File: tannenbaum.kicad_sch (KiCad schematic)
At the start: 34 parts, among them Q1 MMBT3904-7-F, Q2 MMBT3904-7-F, Q3 MMBT3904-7-F, Q4 MMBT3904-7-F, Q5 2N7002, U1 ICM7555IPAZ

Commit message: nets
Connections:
- net V2 2-3: now reaches D10.2 (A), D6.1 (K)
- net B1 2-3: now reaches D11.2 (A), D7.1 (K)
- net B1 1-2: now reaches D3.1 (K), D7.2 (A)
- net B2 2-3: now reaches D12.2 (A), D8.1 (K)
- net V2 1-2: now reaches D2.1 (K), D6.2 (A)
- net V1 2-3: now reaches D5.1 (K), D9.2 (A)
- net B2 1-2: now reaches D4.1 (K), D8.2 (A)
- net V1 1-2: now reaches D1.1 (K), D5.2 (A)
- net CV1 renamed CCV1
- net CV2 renamed CCV2
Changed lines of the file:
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@@
+    (stroke (width 0) (type default))
+  )
+  (wire (pts (xy 124.46 41.91) (xy 124.46 46.99))
     (stroke (width 0) (type default))
   )
@@
     (stroke (width 0) (type default))
   )
-  (wire (pts (xy 124.46 41.91) (xy 124.46 46.99))
-    (stroke (width 0) (type default))
-  )
   (wire (pts (xy 256.54 54.61) (xy 256.54 60.96))
     (stroke (width 0) (type default))
@@
     (stroke (width 0) (type default))
   )
-  (wire (pts (xy 116.84 66.04) (xy 130.81 66.04))
-    (stroke (width 0) (type default))
-  )
   (wire (pts (xy 69.85 116.84) (xy 69.85 119.38))
     (stroke (width 0) (type default))
@@
   )
   (wire (pts (xy 124.46 27.94) (xy 124.46 34.29))
-    (stroke (width 0) (type default))
-  )
-  (wire (pts (xy 139.7 66.04) (xy 153.67 66.04))
     (stroke (width 0) (type default))
   )
@@
     (effects (font (size 1.27 1.27)) (justify left bottom))
   )
+  (label "V2 2-3" (at 147.32 45.72 180) (fields_autoplaced)
+    (effects (font (size 1.27 1.27)) (justify right bottom))
+  )
   (label "CMD" (at 180.34 71.12 180) (fields_autoplaced)
     (effects (font (size 1.27 1.27)) (justify right bottom))
   )
+  (label "B2 2-3" (at 256.54 45.72 180) (fields_autoplaced)
+    (effects (font (size 1.27 1.27)) (justify right bottom))
+  )
   (label "{slash}CMD" (at 187.96 62.23 0) (fields_autoplaced)
     (effects (font (size 1.27 1.27)) (justify left bottom))
@@
     (effects (font (size 1.27 1.27)) (justify left bottom))
   )
+  (label "B1 2-3" (at 231.14 45.72 180) (fields_autoplaced)
+    (effects (font (size 1.27 1.27)) (justify right bottom))
+  )
   (label "9V" (at 124.46 20.32 0) (fields_autoplaced)
     (effects (font (size 1.27 1.27)) (justify left bottom))
@@
     (effects (font (size 1.27 1.27)) (justify left bottom))
   )
-  (label "CMD" (at 153.67 66.04 180) (fields_autoplaced)
+  (label "CMD" (at 139.7 66.04 180) (fields_autoplaced)
+    (effects (font (size 1.27 1.27)) (justify right bottom))
+  )
+  (label "B2 1-2" (at 256.54 31.75 180) (fields_autoplaced)
     (effects (font (size 1.27 1.27)) (justify right bottom))
   )
@@
     (effects (font (size 1.27 1.27)) (justify right bottom))
   )
+  (label "V2 1-2" (at 147.32 31.75 180) (fields_autoplaced)
+    (effects (font (size 1.27 1.27)) (justify right bottom))
+  )
   (label "9V" (at 256.54 20.32 0) (fields_autoplaced)
     (effects (font (size 1.27 1.27)) (justify left bottom))
   )
+  (label "V1 1-2" (at 124.46 31.75 180) (fields_autoplaced)
+    (effects (font (size 1.27 1.27)) (justify right bottom))
+  )
   (label "3V3" (at 69.85 90.17 90) (fields_autoplaced)
     (effects (font (size 1.27 1.27)) (justify left bottom))
   )
-  (label "CV2" (at 147.32 59.69 0) (fields_autoplaced)
-    (effects (font (size 1.27 1.27)) (justify left bottom))
-  )
-  (label "CV1" (at 124.46 59.69 0) (fields_autoplaced)
-    (effects (font (size 1.27 1.27)) (justify left bottom))
+  (label "V1 2-3" (at 124.46 45.72 180) (fields_autoplaced)
+    (effects (font (size 1.27 1.27)) (justify right bottom))
+  )
+  (label "CCV2" (at 147.32 59.69 0) (fields_autoplaced)
+    (effects (font (size 1.27 1.27)) (justify left bottom))
+  )
+  (label "CCV1" (at 124.46 59.69 0) (fields_autoplaced)
+    (effects (font (size 1.27 1.27)) (justify left bottom))
+  )
+  (label "B1 1-2" (at 231.14 31.75 180) (fields_autoplaced)
+    (effects (font (size 1.27 1.27)) (justify right bottom))
   )
   (label "9V" (at 147.32 20.32 0) (fields_autoplaced)
@@
     (effects (font (size 1.27 1.27)) (justify right bottom))
   )
-  (label "CMD" (at 130.81 66.04 180) (fields_autoplaced)
+  (label "CMD" (at 116.84 66.04 180) (fields_autoplaced)
     (effects (font (size 1.27 1.27)) (justify right bottom))
   )
@@
   (symbol (lib_id "dk_Transistors-Bipolar-BJT-Single:MMBT3904-7-F") (at 121.92 66.04 0) (unit 1)
     (in_bom yes) (on_board yes) (dnp no)
-    (property "Reference" "Q1" (at 127 64.77 0)
+    (property "Reference" "Q1" (at 127 67.31 0)
       (effects (font (size 1.524 1.524)) (justify left))
     )

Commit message: pcb
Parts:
- removed U1: ICM7555IPAZ, digikey-footprints:DIP-8_W7.62mm, symbol dk_Clock-Timing-Programmable-Timers-and-Oscillators:ICM7555IPAZ
- added U1: ICM7555xB, Package_SO:SOIC-8_3.9x4.9mm_P1.27mm, symbol Timer:ICM7555xB
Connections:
- net 3V3: now also U1.4 (R), U1.8 (VCC)
- net CMD: now also R12.1; no longer R12.2
- net DSC: now also U1.7 (DIS)
- net GND: now also U1.1 (GND)
- net THR: now also U1.2 (TR), U1.6 (THR)
- net at C2.1: now also U1.5 (CV)
- new net: R12.2, U1.3 (Q)
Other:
- moved on the sheet: C1, C2, C3, D13, R10, R11, R12

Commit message: corretti simboli
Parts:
- D1, D10, D11, D12, D2, D3, D4, D5, D6, D7, D8, D9: footprint LED_SMD:LED_0805_2012Metric -> LED_SMD:LED_0805_2012Metric_LW
- R5, R6, R7, R8: footprint PVG5A202C03R00:TRIM_PVG5A202C03R00 -> PVG5A202C03R00:TRIM_PVG5A202C03R00_TWO; symbol Device:R_Trim -> Device:R_Trim_OK_NC
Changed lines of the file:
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@@
       (effects (font (size 1.27 1.27)))
     )
-    (property "Footprint" "LED_SMD:LED_0805_2012Metric" (at 147.32 50.8 0)
+    (property "Footprint" "LED_SMD:LED_0805_2012Metric_LW" (at 147.32 50.8 0)
       (effects (font (size 1.27 1.27)) hide)
     )
@@
       (effects (font (size 1.27 1.27)))
     )
-    (property "Footprint" "LED_SMD:LED_0805_2012Metric" (at 231.14 38.1 0)
+    (property "Footprint" "LED_SMD:LED_0805_2012Metric_LW" (at 231.14 38.1 0)
       (effects (font (size 1.27 1.27)) hide)
     )
@@
     )
   )
-  (symbol (lib_id "Device:R_Trim") (at 147.32 88.9 0) (unit 1)
+  (symbol (lib_id "Device:R_Trim_OK_NC") (at 147.32 88.9 0) (unit 1)
     (in_bom yes) (on_board yes) (dnp no)
     (property "Reference" "R6" (at 151.13 87.63 0)
@@
       (effects (font (size 1.27 1.27)) (justify left))
     )
-    (property "Footprint" "PVG5A202C03R00:TRIM_PVG5A202C03R00" (at 145.542 88.9 90)
+    (property "Footprint" "PVG5A202C03R00:TRIM_PVG5A202C03R00_TWO" (at 145.542 88.9 90)
       (effects (font (size 1.27 1.27)) hide)
     )
@@
     (pin "1")
     (pin "2")
+    (pin "3")
     (instances
       (project "tannenbaum"
@@
       (effects (font (size 1.27 1.27)))
     )
-    (property "Footprint" "LED_SMD:LED_0805_2012Metric" (at 231.14 50.8 0)
+    (property "Footprint" "LED_SMD:LED_0805_2012Metric_LW" (at 231.14 50.8 0)
       (effects (font (size 1.27 1.27)) hide)
     )
@@
       (effects (font (size 1.27 1.27)))
     )
-    (property "Footprint" "LED_SMD:LED_0805_2012Metric" (at 256.54 50.8 0)
+    (property "Footprint" "LED_SMD:LED_0805_2012Metric_LW" (at 256.54 50.8 0)
       (effects (font (size 1.27 1.27)) hide)
     )
@@
     )
   )
-  (symbol (lib_id "Device:R_Trim") (at 124.46 88.9 0) (unit 1)
+  (symbol (lib_id "Device:R_Trim_OK_NC") (at 124.46 88.9 0) (unit 1)
     (in_bom yes) (on_board yes) (dnp no)
     (property "Reference" "R5" (at 128.27 87.63 0)
@@
       (effects (font (size 1.27 1.27)) (justify left))
     )
-    (property "Footprint" "PVG5A202C03R00:TRIM_PVG5A202C03R00" (at 122.682 88.9 90)
+    (property "Footprint" "PVG5A202C03R00:TRIM_PVG5A202C03R00_TWO" (at 122.682 88.9 90)
       (effects (font (size 1.27 1.27)) hide)
     )
@@
     (pin "1")
     (pin "2")
+    (pin "3")
     (instances
       (project "tannenbaum"
@@
     )
   )
-  (symbol (lib_id "Device:R_Trim") (at 256.54 88.9 0) (unit 1)
+  (symbol (lib_id "Device:R_Trim_OK_NC") (at 256.54 88.9 0) (unit 1)
     (in_bom yes) (on_board yes) (dnp no)
     (property "Reference" "R8" (at 260.35 87.63 0)
@@
       (effects (font (size 1.27 1.27)) (justify left))
     )
-    (property "Footprint" "PVG5A202C03R00:TRIM_PVG5A202C03R00" (at 254.762 88.9 90)
+    (property "Footprint" "PVG5A202C03R00:TRIM_PVG5A202C03R00_TWO" (at 254.762 88.9 90)
       (effects (font (size 1.27 1.27)) hide)
     )
@@
     (pin "1")
     (pin "2")
+    (pin "3")
     (instances
       (project "tannenbaum"
@@
       (effects (font (size 1.27 1.27)))
     )
-    (property "Footprint" "LED_SMD:LED_0805_2012Metric" (at 147.32 24.13 0)
+    (property "Footprint" "LED_SMD:LED_0805_2012Metric_LW" (at 147.32 24.13 0)
       (effects (font (size 1.27 1.27)) hide)
     )
@@
       (effects (font (size 1.27 1.27)))
     )
-    (property "Footprint" "LED_SMD:LED_0805_2012Metric" (at 124.46 50.8 0)
+    (property "Footprint" "LED_SMD:LED_0805_2012Metric_LW" (at 124.46 50.8 0)
       (effects (font (size 1.27 1.27)) hide)
     )
@@
       (effects (font (size 1.27 1.27)) (justify right))
     )
-    (property "Footprint" "LED_SMD:LED_0805_2012Metric" (at 256.54 24.13 0)
+    (property "Footprint" "LED_SMD:LED_0805_2012Metric_LW" (at 256.54 24.13 0)
       (effects (font (size 1.27 1.27)) hide)
     )
@@
       (effects (font (size 1.27 1.27)))
     )
-    (property "Footprint" "LED_SMD:LED_0805_2012Metric" (at 231.14 24.13 0)
+    (property "Footprint" "LED_SMD:LED_0805_2012Metric_LW" (at 231.14 24.13 0)
       (effects (font (size 1.27 1.27)) hide)
     )
@@
       (effects (font (size 1.27 1.27)))
     )
-    (property "Footprint" "LED_SMD:LED_0805_2012Metric" (at 147.32 38.1 0)
+    (property "Footprint" "LED_SMD:LED_0805_2012Metric_LW" (at 147.32 38.1 0)
       (effects (font (size 1.27 1.27)) hide)
     )
@@
       (effects (font (size 1.27 1.27)))
     )
-    (property "Footprint" "LED_SMD:LED_0805_2012Metric" (at 256.54 38.1 0)
+    (property "Footprint" "LED_SMD:LED_0805_2012Metric_LW" (at 256.54 38.1 0)
       (effects (font (size 1.27 1.27)) hide)
     )
@@
     )
   )
-  (symbol (lib_id "Device:R_Trim") (at 231.14 88.9 0) (unit 1)
+  (symbol (lib_id "Device:R_Trim_OK_NC") (at 231.14 88.9 0) (unit 1)
     (in_bom yes) (on_board yes) (dnp no)
     (property "Reference" "R7" (at 234.95 87.63 0)
@@
       (effects (font (size 1.27 1.27)) (justify left))
     )
-    (property "Footprint" "PVG5A202C03R00:TRIM_PVG5A202C03R00" (at 229.362 88.9 90)
+    (property "Footprint" "PVG5A202C03R00:TRIM_PVG5A202C03R00_TWO" (at 229.362 88.9 90)
       (effects (font (size 1.27 1.27)) hide)
     )
@@
     (pin "1")
     (pin "2")
+    (pin "3")
     (instances
       (project "tannenbaum"
@@
       (effects (font (size 1.27 1.27)))
     )
-    (property "Footprint" "LED_SMD:LED_0805_2012Metric" (at 124.46 38.1 0)
+    (property "Footprint" "LED_SMD:LED_0805_2012Metric_LW" (at 124.46 38.1 0)
       (effects (font (size 1.27 1.27)) hide)
     )
@@
       (effects (font (size 1.27 1.27)))
     )
-    (property "Footprint" "LED_SMD:LED_0805_2012Metric" (at 124.46 24.13 0)
-      (effects (font (size 1.27 1.27)) hide)
-    )
+    (property "Footprint" "LED_SMD:LED_0805_2012Metric_LW" (at 124.46 24.13 0)
+      (effects (font (size 1.27 1.27)) hide)
+    )

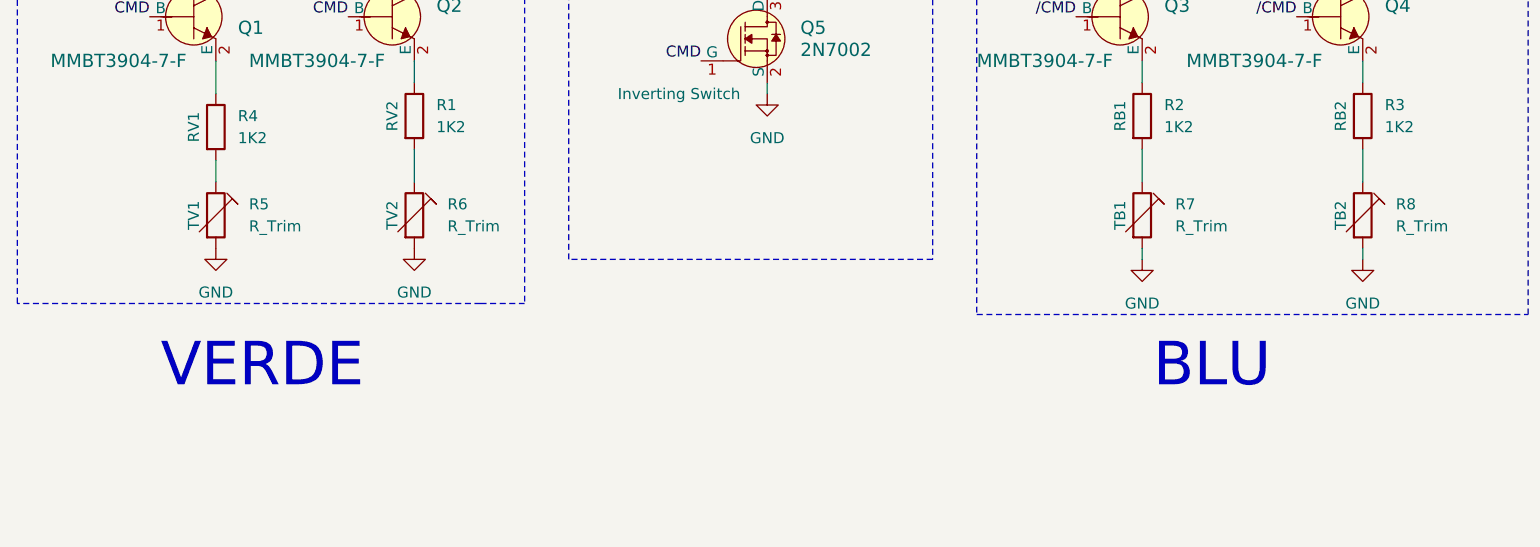
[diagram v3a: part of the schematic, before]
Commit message: corretti impronte
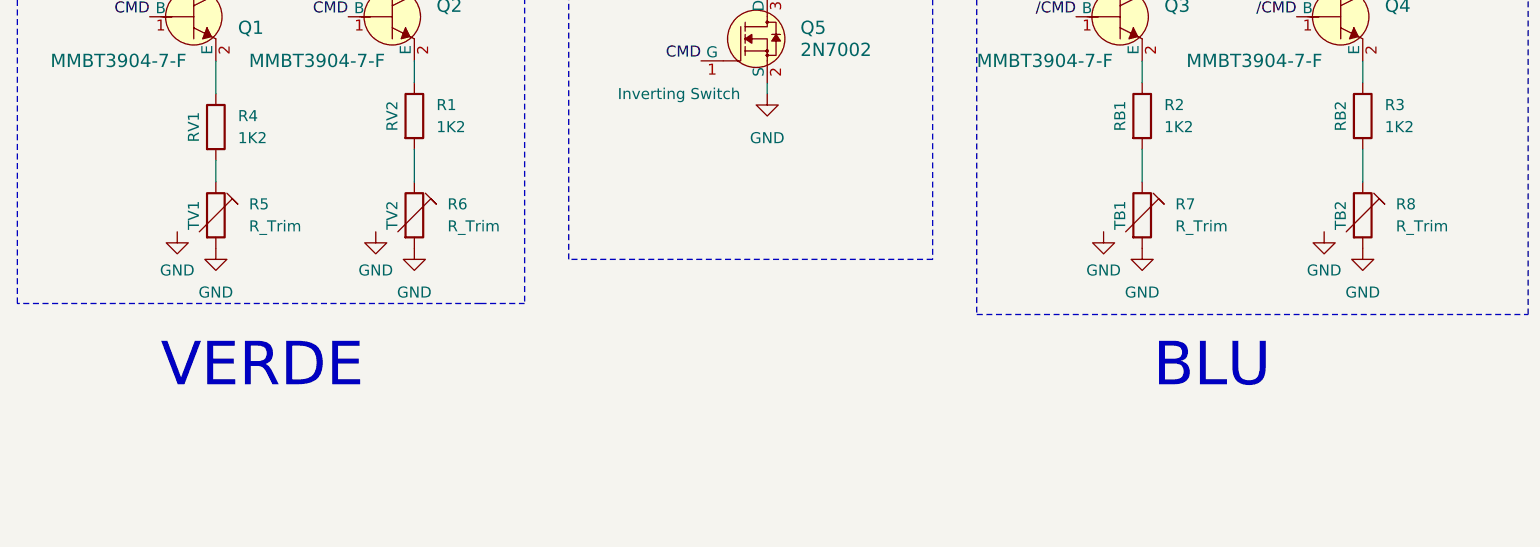
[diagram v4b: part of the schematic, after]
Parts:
- R5, R6, R7, R8: symbol Device:R_Trim_OK_NC -> Device:R_Trim_OK
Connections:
- net GND: now also R5.3, R6.3, R7.3, R8.3
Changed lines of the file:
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@@
     (stroke (width 0) (type dash))
-  )
-  (wire (pts (xy 256.54 92.71) (xy 256.54 93.98))
-    (stroke (width 0) (type default))
   )
   (polyline (pts (xy 160.02 15.24) (xy 160.02 99.06))
@@
   )
   (wire (pts (xy 48.26 83.185) (xy 48.26 92.075))
-    (stroke (width 0) (type default))
-  )
-  (wire (pts (xy 231.14 92.71) (xy 231.14 93.98))
     (stroke (width 0) (type default))
   )
@@
     )
   )
+  (symbol (lib_id "power:GND") (at 142.875 90.805 0) (unit 1)
+    (in_bom yes) (on_board yes) (dnp no) (fields_autoplaced)
+    (property "Reference" "#PWR013" (at 142.875 97.155 0)
+      (effects (font (size 1.27 1.27)) hide)
+    )
+    (property "Value" "GND" (at 142.875 95.25 0)
+      (effects (font (size 1.27 1.27)))
+    )
+    (property "Footprint" "" (at 142.875 90.805 0)
+      (effects (font (size 1.27 1.27)) hide)
+    )
+    (property "Datasheet" "" (at 142.875 90.805 0)
+      (effects (font (size 1.27 1.27)) hide)
+    )
+    (pin "1")
+    (instances
+      (project "tannenbaum"
+        (path "/a6288757-7e9b-4a60-9ecc-2dfb03657791"
+          (reference "#PWR013") (unit 1)
+        )
+      )
+    )
+  )
   (symbol (lib_id "Device:LED") (at 231.14 38.1 90) (unit 1)
     (in_bom yes) (on_board yes) (dnp no)
@@
     )
   )
-  (symbol (lib_id "Device:R_Trim_OK_NC") (at 147.32 88.9 0) (unit 1)
+  (symbol (lib_id "Device:R_Trim_OK") (at 147.32 88.9 0) (unit 1)
     (in_bom yes) (on_board yes) (dnp no)
     (property "Reference" "R6" (at 151.13 87.63 0)
@@
     )
   )
-  (symbol (lib_id "Device:R_Trim_OK_NC") (at 124.46 88.9 0) (unit 1)
+  (symbol (lib_id "Device:R_Trim_OK") (at 124.46 88.9 0) (unit 1)
     (in_bom yes) (on_board yes) (dnp no)
     (property "Reference" "R5" (at 128.27 87.63 0)
@@
         (path "/a6288757-7e9b-4a60-9ecc-2dfb03657791"
           (reference "R5") (unit 1)
+        )
+      )
+    )
+  )
+  (symbol (lib_id "power:GND") (at 120.015 90.805 0) (unit 1)
+    (in_bom yes) (on_board yes) (dnp no) (fields_autoplaced)
+    (property "Reference" "#PWR012" (at 120.015 97.155 0)
+      (effects (font (size 1.27 1.27)) hide)
+    )
+    (property "Value" "GND" (at 120.015 95.25 0)
+      (effects (font (size 1.27 1.27)))
+    )
+    (property "Footprint" "" (at 120.015 90.805 0)
+      (effects (font (size 1.27 1.27)) hide)
+    )
+    (property "Datasheet" "" (at 120.015 90.805 0)
+      (effects (font (size 1.27 1.27)) hide)
+    )
+    (pin "1")
+    (instances
+      (project "tannenbaum"
+        (path "/a6288757-7e9b-4a60-9ecc-2dfb03657791"
+          (reference "#PWR012") (unit 1)
         )
       )
@@
     )
   )
-  (symbol (lib_id "Device:R_Trim_OK_NC") (at 256.54 88.9 0) (unit 1)
+  (symbol (lib_id "Device:R_Trim_OK") (at 256.54 88.9 0) (unit 1)
     (in_bom yes) (on_board yes) (dnp no)
     (property "Reference" "R8" (at 260.35 87.63 0)
@@
         (path "/a6288757-7e9b-4a60-9ecc-2dfb03657791"
           (reference "C2") (unit 1)
+        )
+      )
+    )
+  )
+  (symbol (lib_id "power:GND") (at 252.095 90.805 0) (unit 1)
+    (in_bom yes) (on_board yes) (dnp no) (fields_autoplaced)
+    (property "Reference" "#PWR015" (at 252.095 97.155 0)
+      (effects (font (size 1.27 1.27)) hide)
+    )
+    (property "Value" "GND" (at 252.095 95.25 0)
+      (effects (font (size 1.27 1.27)))
+    )
+    (property "Footprint" "" (at 252.095 90.805 0)
+      (effects (font (size 1.27 1.27)) hide)
+    )
+    (property "Datasheet" "" (at 252.095 90.805 0)
+      (effects (font (size 1.27 1.27)) hide)
+    )
+    (pin "1")
+    (instances
+      (project "tannenbaum"
+        (path "/a6288757-7e9b-4a60-9ecc-2dfb03657791"
+          (reference "#PWR015") (unit 1)
         )
       )
@@
     )
   )
+  (symbol (lib_id "power:GND") (at 226.695 90.805 0) (unit 1)
+    (in_bom yes) (on_board yes) (dnp no) (fields_autoplaced)
+    (property "Reference" "#PWR014" (at 226.695 97.155 0)
+      (effects (font (size 1.27 1.27)) hide)
+    )
+    (property "Value" "GND" (at 226.695 95.25 0)
+      (effects (font (size 1.27 1.27)))
+    )
+    (property "Footprint" "" (at 226.695 90.805 0)
+      (effects (font (size 1.27 1.27)) hide)
+    )
+    (property "Datasheet" "" (at 226.695 90.805 0)
+      (effects (font (size 1.27 1.27)) hide)
+    )
+    (pin "1")
+    (instances
+      (project "tannenbaum"
+        (path "/a6288757-7e9b-4a60-9ecc-2dfb03657791"
+          (reference "#PWR014") (unit 1)
+        )
+      )
+    )
+  )
   (symbol (lib_id "power:GND") (at 147.32 92.71 0) (unit 1)
     (in_bom yes) (on_board yes) (dnp no) (fields_autoplaced)
@@
     )
   )
-  (symbol (lib_id "Device:R_Trim_OK_NC") (at 231.14 88.9 0) (unit 1)
+  (symbol (lib_id "Device:R_Trim_OK") (at 231.14 88.9 0) (unit 1)
     (in_bom yes) (on_board yes) (dnp no)
     (property "Reference" "R7" (at 234.95 87.63 0)
@@
     )
   )
-  (symbol (lib_id "power:GND") (at 231.14 93.98 0) (unit 1)
+  (symbol (lib_id "power:GND") (at 231.14 92.71 0) (unit 1)
     (in_bom yes) (on_board yes) (dnp no) (fields_autoplaced)
-    (property "Reference" "#PWR05" (at 231.14 100.33 0)
-      (effects (font (size 1.27 1.27)) hide)
-    )
-    (property "Value" "GND" (at 231.14 99.06 0)
-      (effects (font (size 1.27 1.27)))
-    )
-    (property "Footprint" "" (at 231.14 93.98 0)
-      (effects (font (size 1.27 1.27)) hide)
-    )
-    (property "Datasheet" "" (at 231.14 93.98 0)
+    (property "Reference" "#PWR05" (at 231.14 99.06 0)
+      (effects (font (size 1.27 1.27)) hide)
+    )
+    (property "Value" "GND" (at 231.14 97.79 0)
+      (effects (font (size 1.27 1.27)))
+    )
+    (property "Footprint" "" (at 231.14 92.71 0)
+      (effects (font (size 1.27 1.27)) hide)
+    )
+    (property "Datasheet" "" (at 231.14 92.71 0)
       (effects (font (size 1.27 1.27)) hide)
     )
@@
     )
   )
-  (symbol (lib_id "power:GND") (at 256.54 93.98 0) (unit 1)
+  (symbol (lib_id "power:GND") (at 256.54 92.71 0) (unit 1)
     (in_bom yes) (on_board yes) (dnp no) (fields_autoplaced)
-    (property "Reference" "#PWR06" (at 256.54 100.33 0)
-      (effects (font (size 1.27 1.27)) hide)
-    )
-    (property "Value" "GND" (at 256.54 99.06 0)
-      (effects (font (size 1.27 1.27)))
-    )
-    (property "Footprint" "" (at 256.54 93.98 0)
-      (effects (font (size 1.27 1.27)) hide)
-    )
-    (property "Datasheet" "" (at 256.54 93.98 0)
-      (effects (font (size 1.27 1.27)) hide)
-    )
+    (property "Reference" "#PWR06" (at 256.54 99.06 0)
+      (effects (font (size 1.27 1.27)) hide)
+    )
+    (property "Value" "GND" (at 256.54 97.79 0)
+      (effects (font (size 1.27 1.27)))
+    )
+    (property "Footprint" "" (at 256.54 92.71 0)
+      (effects (font (size 1.27 1.27)) hide)
+    )
+    (property "Datasheet" "" (at 256.54 92.71 0)
+      (effects (font (size 1.27 1.27)) hide)
+    )

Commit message: gerber
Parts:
- added D10, D17, D18, D19, D8, D9: LED, LED_SMD:LED_0805_2012Metric_LW, symbol Device:LED
- added Q3, Q7: MMBT3904-7-F, digikey-footprints:SOT-23-3, symbol dk_Transistors-Bipolar-BJT-Single:MMBT3904-7-F
- added R15, R8: 1K2, Resistor_SMD:R_0603_1608Metric, symbol Device:R
- added R16, R9: R_Trim, Potentiometer_SMD:Potentiometer_Bourns_TC33X_Vertical, symbol Device:R_Trim_OK
- R12: renamed from R7; footprint PVG5A202C03R00:TRIM_PVG5A202C03R00_TWO -> Potentiometer_SMD:Potentiometer_Bourns_TC33X_Vertical
- R14: renamed from R8; footprint PVG5A202C03R00:TRIM_PVG5A202C03R00_TWO -> Potentiometer_SMD:Potentiometer_Bourns_TC33X_Vertical
- R5: footprint PVG5A202C03R00:TRIM_PVG5A202C03R00_TWO -> Potentiometer_SMD:Potentiometer_Bourns_TC33X_Vertical
- R7: renamed from R6; footprint PVG5A202C03R00:TRIM_PVG5A202C03R00_TWO -> Potentiometer_SMD:Potentiometer_Bourns_TC33X_Vertical
- renumbered C2 to C1, C1 to C2, D13 to D1, D3 to D11, D7 to D12, D11 to D13, D4 to D14, D8 to D15, D12 to D16, D1 to D2, D5 to D3, D9 to D4, D2 to D5, D10 to D7, Q5 to Q4, Q3 to Q5, Q4 to Q6, R12 to R1, R9 to R10, R2 to R11, R3 to R13, R11 to R2, R10 to R3, R1 to R6
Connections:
- net 9V: now also D17.2 (A), D8.2 (A)
- net CMD: now also Q3.1 (B)
- net GND: now also R16.2, R16.3, R9.2, R9.3
- net /CMD: now also Q7.1 (B)
- new net: Q7.2 (E), R15.1
- new net: Q3.2 (E), R8.1
- new net: R8.2, R9.1
- new net: R15.2, R16.1
- new net B3 1-2: D17.1 (K), D18.2 (A)
- new net B3 2-3: D18.1 (K), D19.2 (A)
- new net CB3: D19.1 (K), Q7.3 (C)
- new net CCV3: D10.1 (K), Q3.3 (C)
- new net V3 1-2: D8.1 (K), D9.2 (A)
- new net V3 2-3: D10.2 (A), D9.1 (K)
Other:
- moved on the sheet: D11, D12, D13, D14, D15, D16, Q4, Q5, Q6, R10, R11, R12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
